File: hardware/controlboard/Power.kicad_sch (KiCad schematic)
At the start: 37 parts, among them J11 Pololu Voltage Regulator, J4 TYPE-C-31-M-12, J7 Screw_Terminal_01x02, J9 mini560 voltage regulator, Q2 PMOS AO3401A, U4 CH224K

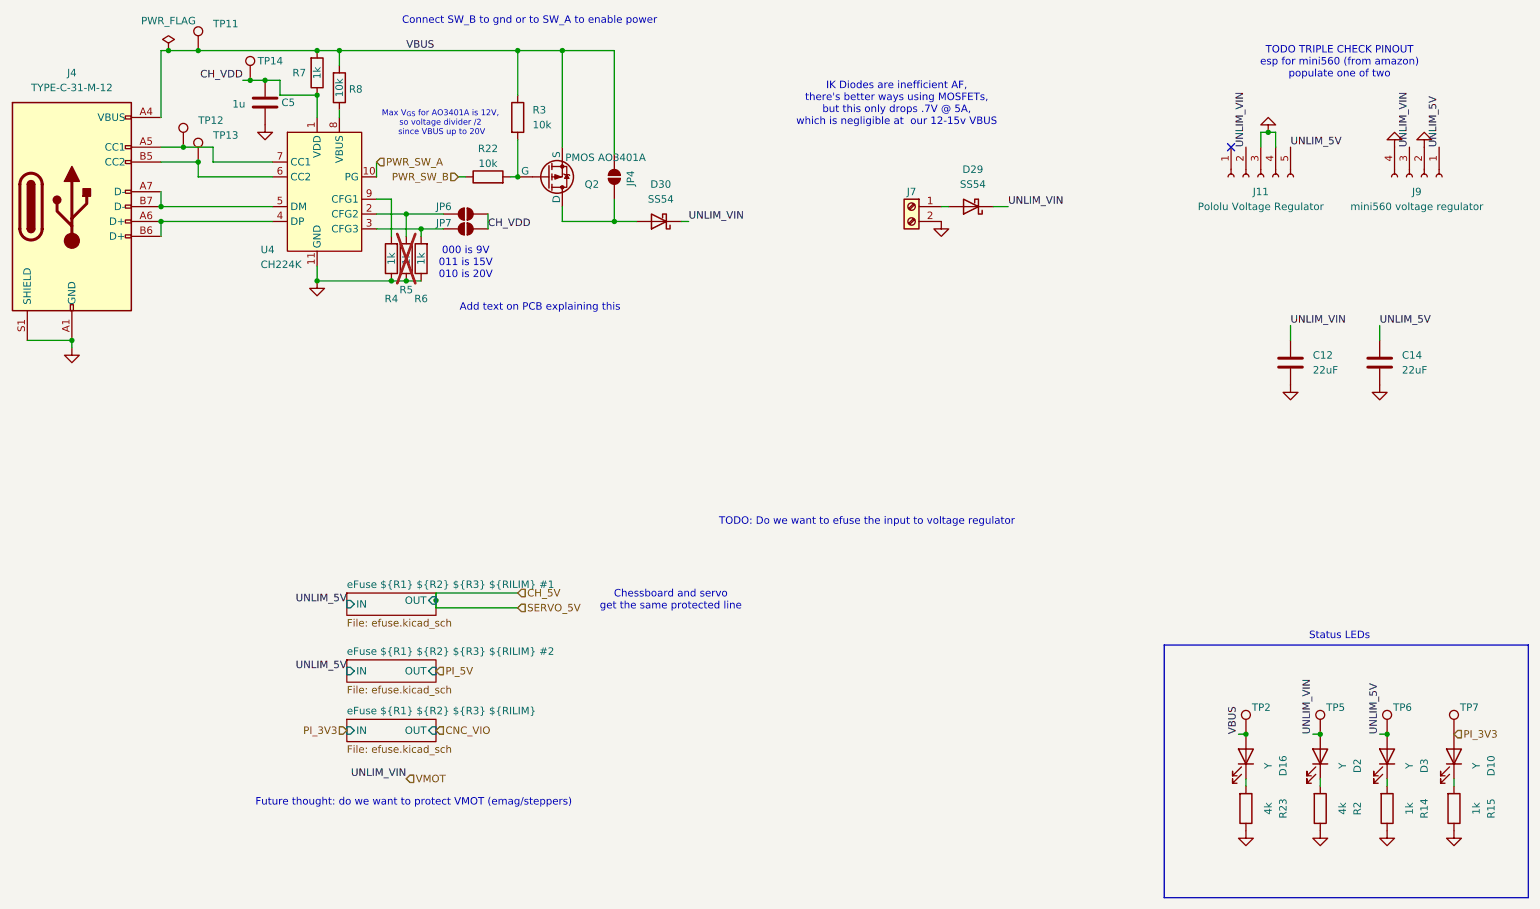
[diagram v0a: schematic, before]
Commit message: Revert controlboard to June 12th 2024
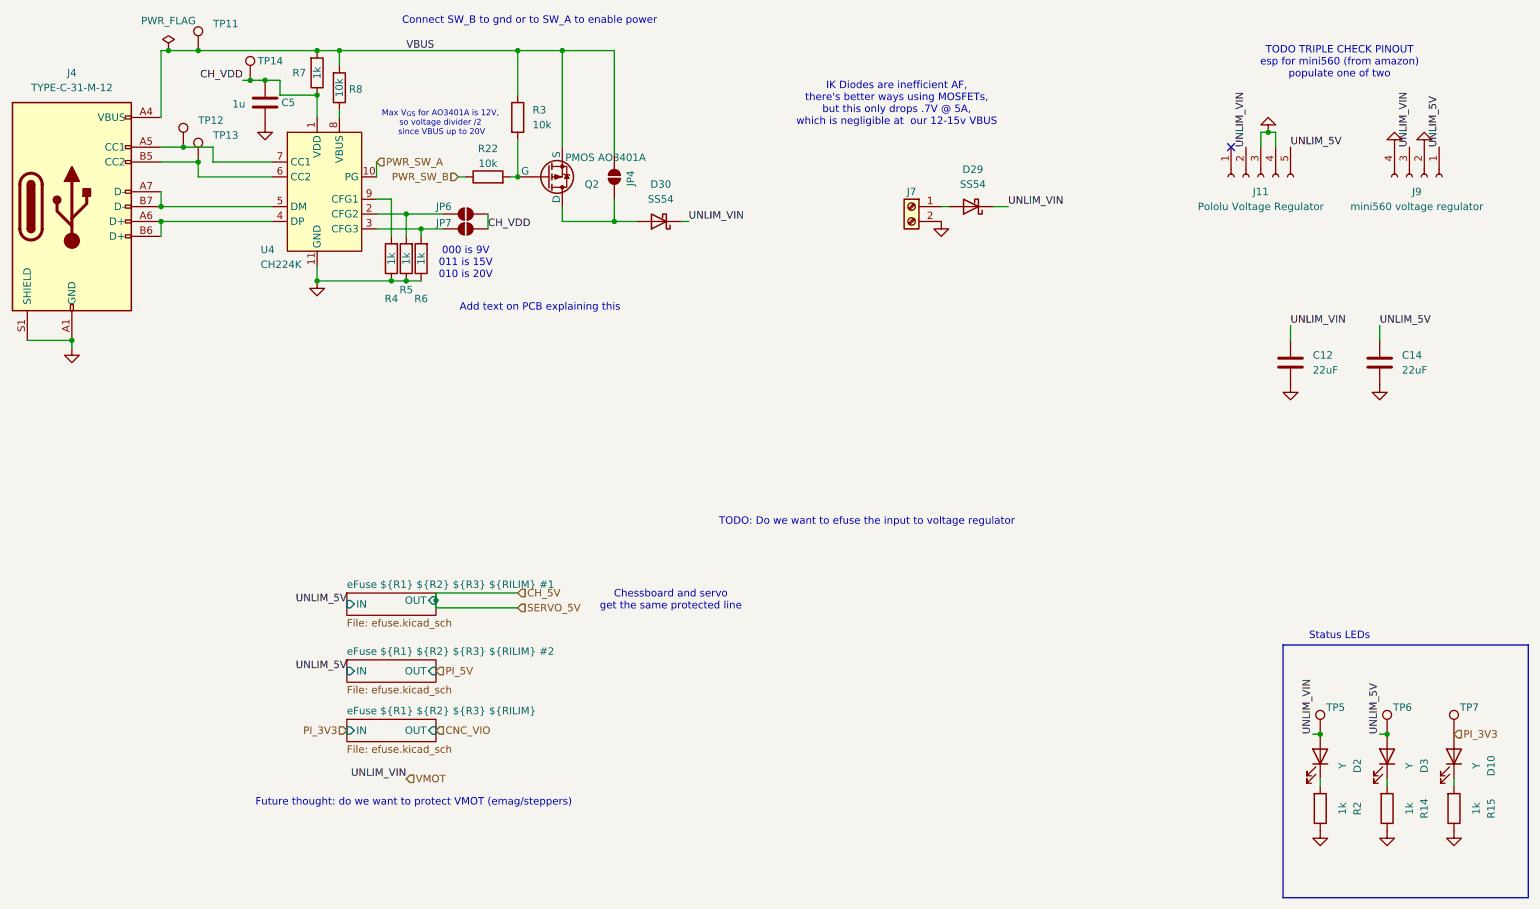
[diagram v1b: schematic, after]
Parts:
- removed D16: Y, LED_SMD:LED_0603_1608Metric_Pad1.05x0.95mm_HandSolder, symbol Device:LED
- removed R23: 4k, Resistor_SMD:R_0603_1608Metric_Pad0.98x0.95mm_HandSolder, symbol Device:R
- removed TP2: TestPoint, TestPoint:TestPoint_THTPad_D2.0mm_Drill1.0mm, symbol Connector:TestPoint
- R2: value 4k -> 1k
- R5: now fitted
